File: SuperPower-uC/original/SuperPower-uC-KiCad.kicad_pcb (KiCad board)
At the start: 2 copper layers, 95 x 42 mm, 168 parts, among them J1 JST_PH_S2B_thru, J2 Barrel_Jack_Switch, J3 Conn_01x02_Male, J4 DNP/JST_ZH_S2B_thru, J5 JST_XH_S2B_thru, J6 Conn_01x02_Male, J7 mcu_pinout, J8 mcu_pinout, Q1 DMN2019UTS, Q10 2N7002A, Q11 2N7002A, Q12 DMP2035UVT, Q13 DMP2035UVT, Q14 DMP2035UVT, Q2 DMP3028LSD, Q3 DMN3018SSD, Q4 2N7002A, Q5 DMP2035UVT, Q6 BSS84-7-F, Q7 S8050, Q8 S8050, Q9 2N7002A, SW1 DNP/SKRKAEE020, U1 AP9101CK6-AYTRG1, U10 TPS63070RNMT, U2 USB-C, U3 IP4220CZ6, U4 LTC4162EUFD-LAD, U5 RV-3028-C7, U6 CP2102N-A01-GQFN28, U7 ESP32-WROOM32, U8 TPS70933DRVT, U9 TPS63070RNMT

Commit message: Update DMN3018SSD SO-8 3D Package
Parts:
- Q3: footprint Package_SO:SO-8_3.9x4.9mm_P1.27mm -> DMN3018SSD:SO-8_3.9x4.9mm_P1.27mm

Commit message: Update 18650 Battery Holder 3D Model
+ Board 3D Model + 3D box
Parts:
- BT1: footprint Battery:BatteryHolder_Keystone_1042_1x18650 -> BATTERY_CELL_HOLDER_18650_SMT_1042:BatteryHolder_Keystone_1042_1x18650

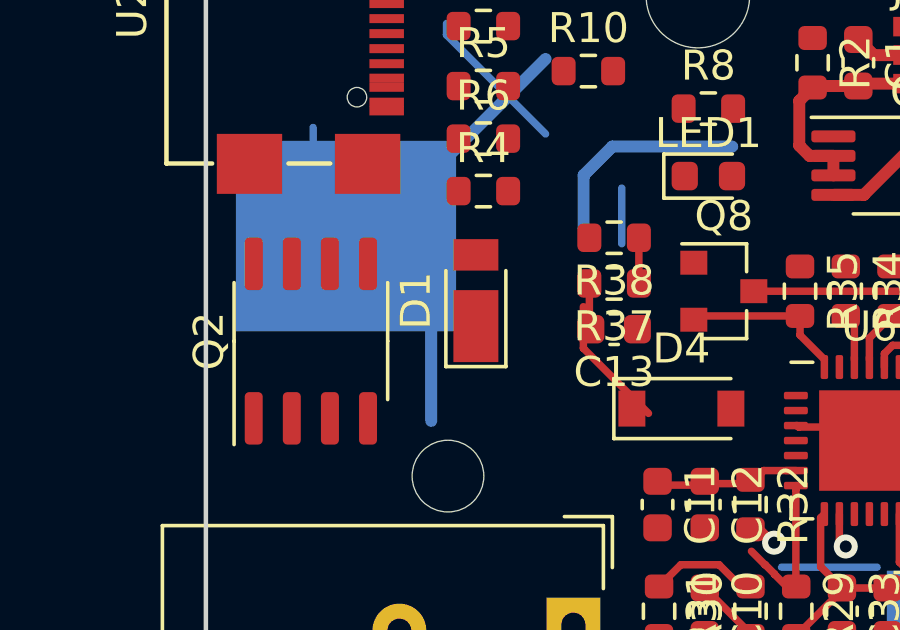
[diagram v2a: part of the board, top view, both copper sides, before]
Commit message: Add a second optional Schottky diode for High Current
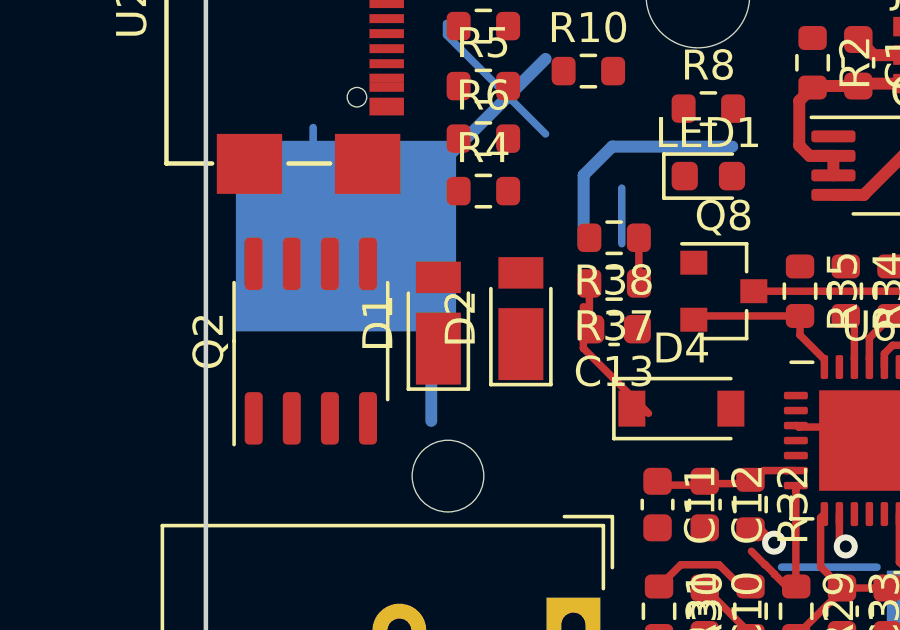
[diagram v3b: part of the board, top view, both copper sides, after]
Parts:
- added D2: DFLS230L, Diode_SMD:D_PowerDI-123, F.Cu at (120.5, 57.8)
- moved D1 1.46 mm to (117.8, 57.9)

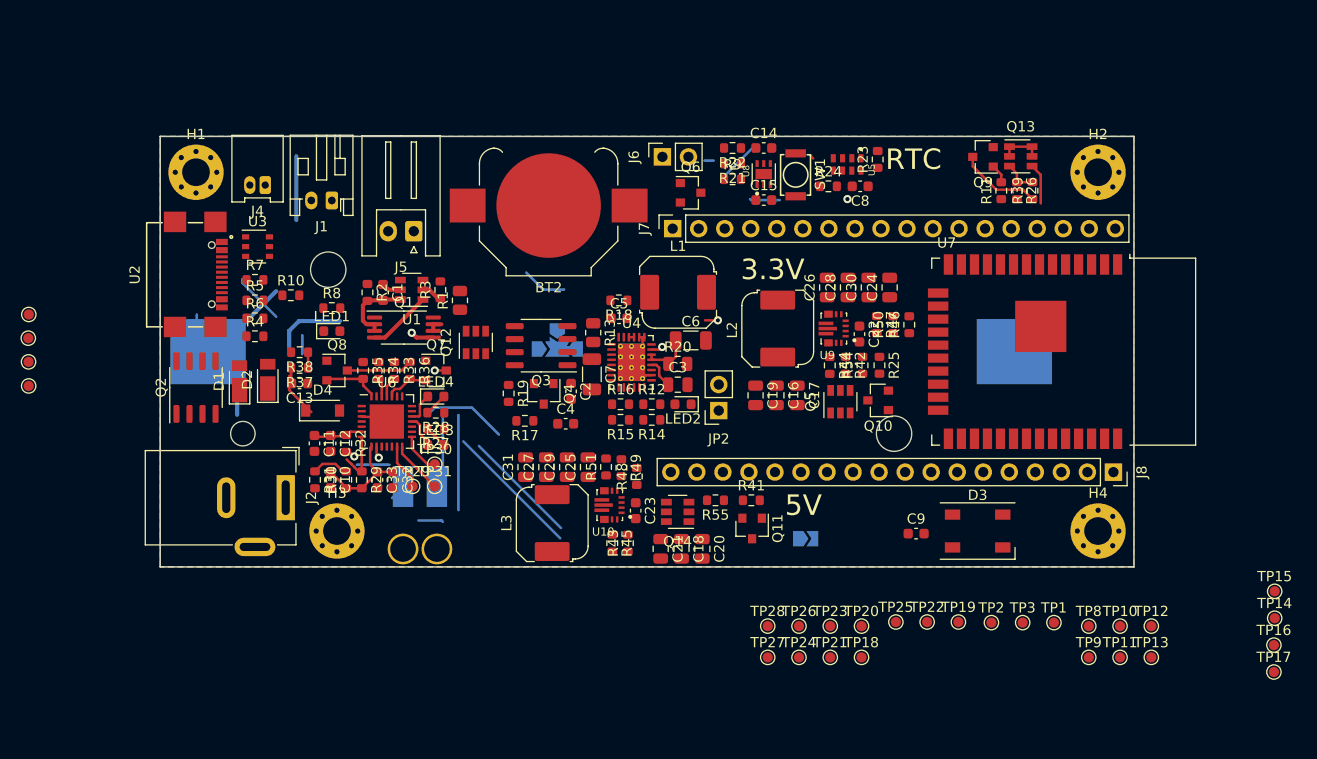
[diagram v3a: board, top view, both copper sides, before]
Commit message: Update components Placement
RTC + 3.3 LDO + single raw connectors (x2)
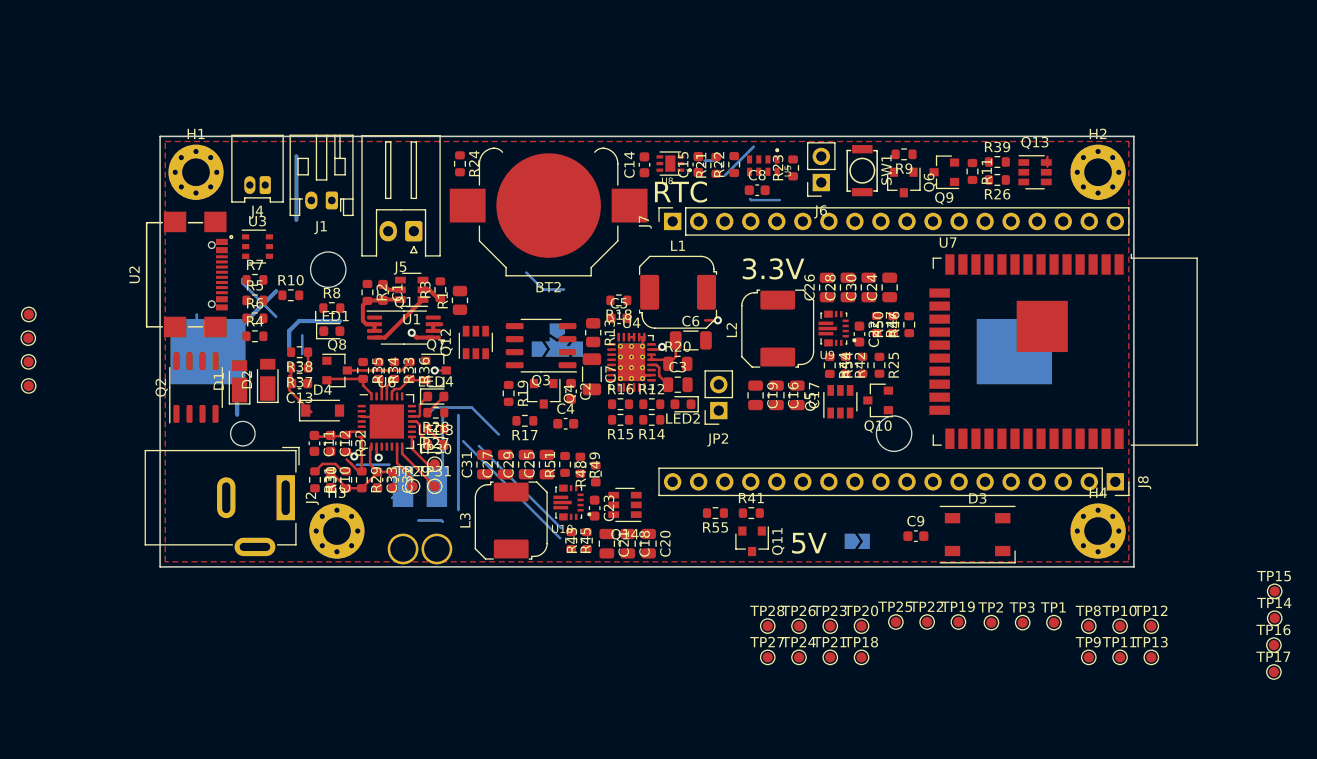
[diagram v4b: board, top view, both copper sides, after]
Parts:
- moved R24 36.0 mm to (139.2, 36.7), turned to 270 degrees
- moved Q6 20.8 mm to (182.6, 38.5), turned to 270 degrees
- moved R9 16.9 mm to (182.6, 35.8), turned to 180 degrees
- moved J6 15.7 mm to (174.5, 38.5), turned to 180 degrees
- moved C14 11.8 mm to (157.2, 36.8), turned to 90 degrees
- moved C8 10.1 mm to (168.2, 39.2), turned to 0 degrees
- moved U8 9.17 mm to (159.8, 36.6), turned to 180 degrees
- moved R23 8.29 mm to (171.8, 37.1)
- moved U5 8.17 mm to (168.8, 36.9)
- moved C15 7.27 mm to (162.5, 36.8), turned to 90 degrees
- moved SW1 6.51 mm to (178.5, 37.3)
- moved C18 5.27 mm to (155.6, 73.7)
- moved C20 5.27 mm to (157.6, 73.7)
- moved C21 5.27 mm to (153.6, 73.7)
- moved Q14 5.18 mm to (155.3, 70.0)
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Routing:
- net Net-(Q9-Pad3): track 8.07 -> 0.00 mm
- net /MCU Module/3v3_MCU: track 5.95 -> 1.52 mm
- net Net-(Q13-Pad3): track 3.40 -> 0.00 mm
- net /MCU Module/3v3: track 4.10 -> 0.95 mm
- net /MCU Module/EN_3V3: track 1.85 -> 0.00 mm
- net /Charging Module/3v3_I2C: vias 1 -> 0

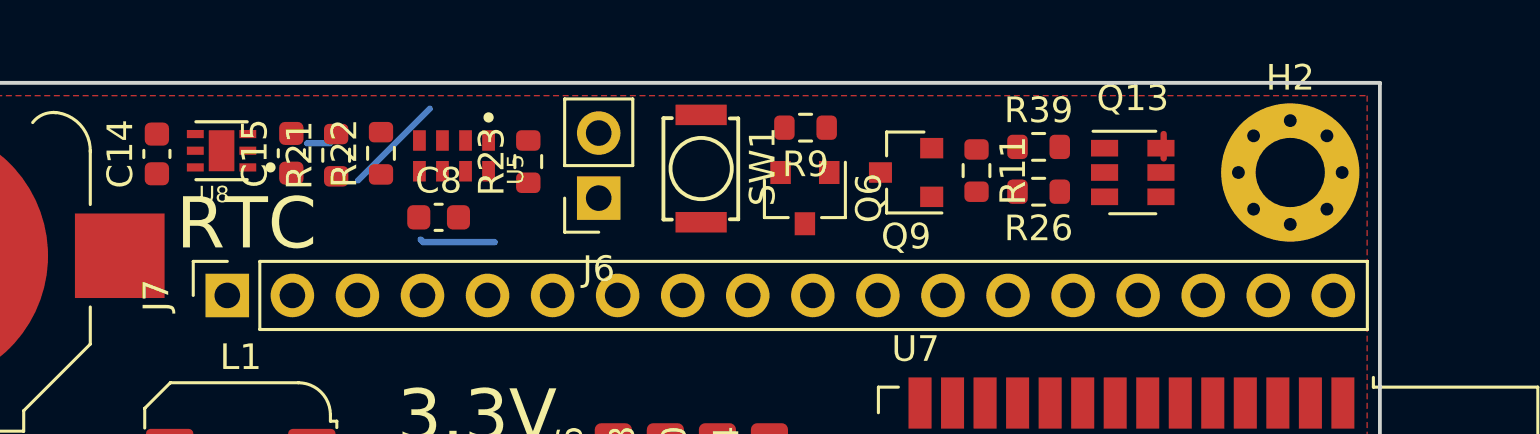
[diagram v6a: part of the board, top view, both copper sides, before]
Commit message: Update TPS709xx series 3D footprint
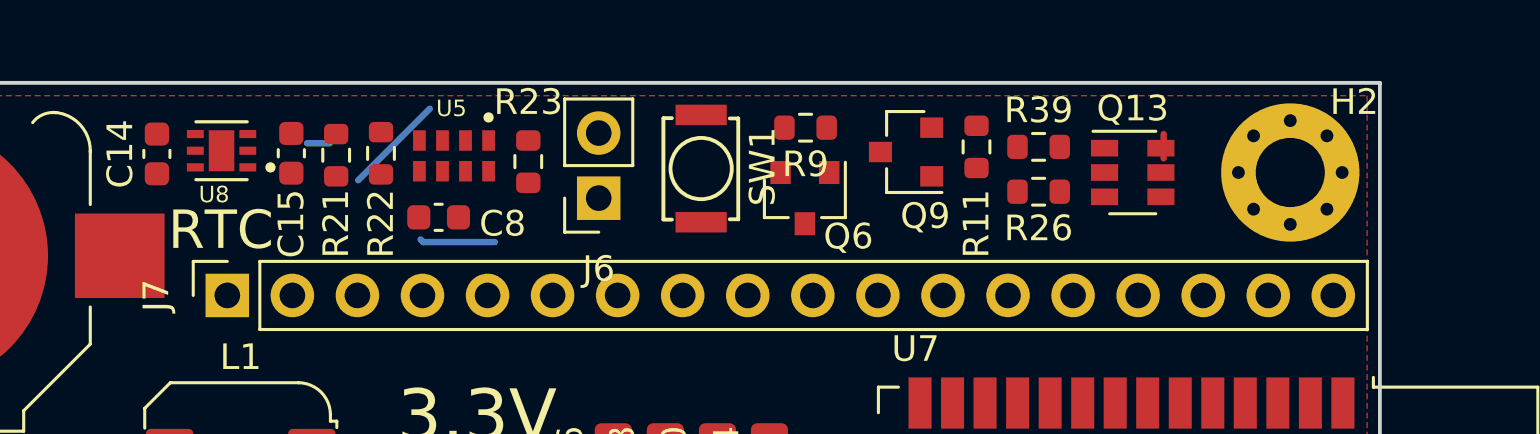
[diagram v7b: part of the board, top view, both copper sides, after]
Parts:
- moved R11 0.92 mm to (189.2, 36.5)
- moved Q9 0.80 mm to (186.5, 36.7)
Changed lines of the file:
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@@
     (uvia_drill 0.1)
   )
+  (module TPS70933DRV:SON65P200X200X80-7N (layer F.Cu)
+    (at 159.775 36.65 180)
+    (fp_text reference U8 (at 0.292 -1.7134) (layer F.SilkS)
+      (effects (font (size 0.64 0.64) (thickness 0.015)))
+    )
+    (fp_text value TPS70933DRVT (at 5.9816 1.7134) (layer F.Fab)
+      (effects (font (size 0.64 0.64) (thickness 0.015)))
+    )
+    (fp_poly (pts (xy -0.316 -0.506) (xy 0.316 -0.506) (xy 0.316 0.506) (xy -0.316 0.506)) (layer F.Paste) (width 0.01))
+    (fp_line (start 1.675 -1.25) (end 1.675 1.25) (layer F.CrtYd) (width 0.05))
+    (fp_line (start -1.675 -1.25) (end -1.675 1.25) (layer F.CrtYd) (width 0.05))
+    (fp_line (start -1.675 1.25) (end 1.675 1.25) (layer F.CrtYd) (width 0.05))
+    (fp_line (start -1.675 -1.25) (end 1.675 -1.25) (layer F.CrtYd) (width 0.05))
+    (fp_line (start 1 -1) (end 1 1) (layer F.Fab) (width 0.127))
+    (fp_line (start -1 -1) (end -1 1) (layer F.Fab) (width 0.127))
+    (fp_line (start -1 1.13) (end 1 1.13) (layer F.SilkS) (width 0.127))
+    (fp_line (start -1 -1.13) (end 1 -1.13) (layer F.SilkS) (width 0.127))
+    (fp_line (start -1 1) (end 1 1) (layer F.Fab) (width 0.127))
+    (fp_line (start -1 -1) (end 1 -1) (layer F.Fab) (width 0.127))
+    (fp_circle (center -1.91 -0.65) (end -1.81 -0.65) (layer F.Fab) (width 0.2))
+    (fp_circle (center -1.91 -0.65) (end -1.81 -0.65) (layer F.SilkS) (width 0.2))
+    (pad 7 smd rect (at 0 0 180) (size 1 1.6) (layers F.Cu F.Mask))
+    (pad 6 smd rect (at 1.025 -0.65 180) (size 0.66 0.32) (layers F.Cu F.Paste F.Mask)
+      (net 133 /RTC/VIN))
+    (pad 5 smd rect (at 1.025 0 180) (size 0.66 0.32) (layers F.Cu F.Paste F.Mask))
+    (pad 4 smd rect (at 1.025 0.65 180) (size 0.66 0.32) (layers F.Cu F.Paste F.Mask)
+      (net 127 "Net-(U8-Pad4)"))
+    (pad 3 smd rect (at -1.025 0.65 180) (size 0.66 0.32) (layers F.Cu F.Paste F.Mask)
+      (net 4 GND))
+    (pad 2 smd rect (at -1.025 0 180) (size 0.66 0.32) (layers F.Cu F.Paste F.Mask))
+    (pad 1 smd rect (at -1.025 -0.65 180) (size 0.66 0.32) (layers F.Cu F.Paste F.Mask)
+      (net 14 "/Charging Module/3v3_I2C"))
+    (model ${KISYS3DMOD}/Package_SON.3dshapes/WSON-6-1EP_2x2mm_P0.65mm_EP1x1.6mm.step
+      (at (xyz 0 0 0))
+      (scale (xyz 1 1 1))
+      (rotate (xyz 0 0 0))
+    )
+  )
   (module RV-3028-C7:IC_RV-3028-C7 (layer F.Cu)
     (at 168.85 36.85 270)
-    (fp_text reference U5 (at 0.532 -2.4064 90) (layer F.SilkS)
+    (fp_text reference U5 (at -1.85 0.1 180) (layer F.SilkS)
       (effects (font (size 0.64 0.64) (thickness 0.015)))
     )
@@
     (tags SOT-23-6)
     (attr smd)
-    (fp_text reference Q13 (at 0 -2.9) (layer F.SilkS)
+    (fp_text reference Q13 (at 0 -2.5) (layer F.SilkS)
       (effects (font (size 1 1) (thickness 0.15)))
     )
@@
     )
   )
-  (module TPS70933DRV:SON65P200X200X80-7N (layer F.Cu)
-    (at 159.775 36.65 180)
-    (fp_text reference U8 (at 0.292 -1.7134) (layer F.SilkS)
-      (effects (font (size 0.64 0.64) (thickness 0.015)))
-    )
-    (fp_text value TPS70933DRVT (at 5.9816 1.7134) (layer F.Fab)
-      (effects (font (size 0.64 0.64) (thickness 0.015)))
-    )
-    (fp_poly (pts (xy -0.316 -0.506) (xy 0.316 -0.506) (xy 0.316 0.506) (xy -0.316 0.506)) (layer F.Paste) (width 0.01))
-    (fp_line (start 1.675 -1.25) (end 1.675 1.25) (layer F.CrtYd) (width 0.05))
-    (fp_line (start -1.675 -1.25) (end -1.675 1.25) (layer F.CrtYd) (width 0.05))
-    (fp_line (start -1.675 1.25) (end 1.675 1.25) (layer F.CrtYd) (width 0.05))
-    (fp_line (start -1.675 -1.25) (end 1.675 -1.25) (layer F.CrtYd) (width 0.05))
-    (fp_line (start 1 -1) (end 1 1) (layer F.Fab) (width 0.127))
-    (fp_line (start -1 -1) (end -1 1) (layer F.Fab) (width 0.127))
-    (fp_line (start -1 1.13) (end 1 1.13) (layer F.SilkS) (width 0.127))
-    (fp_line (start -1 -1.13) (end 1 -1.13) (layer F.SilkS) (width 0.127))
-    (fp_line (start -1 1) (end 1 1) (layer F.Fab) (width 0.127))
-    (fp_line (start -1 -1) (end 1 -1) (layer F.Fab) (width 0.127))
-    (fp_circle (center -1.91 -0.65) (end -1.81 -0.65) (layer F.Fab) (width 0.2))
-    (fp_circle (center -1.91 -0.65) (end -1.81 -0.65) (layer F.SilkS) (width 0.2))
-    (pad 7 smd rect (at 0 0 180) (size 1 1.6) (layers F.Cu F.Mask))
-    (pad 6 smd rect (at 1.025 -0.65 180) (size 0.66 0.32) (layers F.Cu F.Paste F.Mask)
-      (net 133 /RTC/VIN))
-    (pad 5 smd rect (at 1.025 0 180) (size 0.66 0.32) (layers F.Cu F.Paste F.Mask))
-    (pad 4 smd rect (at 1.025 0.65 180) (size 0.66 0.32) (layers F.Cu F.Paste F.Mask)
-      (net 127 "Net-(U8-Pad4)"))
-    (pad 3 smd rect (at -1.025 0.65 180) (size 0.66 0.32) (layers F.Cu F.Paste F.Mask)
-      (net 4 GND))
-    (pad 2 smd rect (at -1.025 0 180) (size 0.66 0.32) (layers F.Cu F.Paste F.Mask))
-    (pad 1 smd rect (at -1.025 -0.65 180) (size 0.66 0.32) (layers F.Cu F.Paste F.Mask)
-      (net 14 "/Charging Module/3v3_I2C"))
-  )
   (module Resistor_SMD:R_0603_1608Metric (layer F.Cu)
     (at 191.675 36.5)
@@
   )
   (module Resistor_SMD:R_0603_1608Metric (layer F.Cu)
-    (at 189.25 37.425 270)
+    (at 189.25 36.5 270)
     (descr "Resistor SMD 0603 (1608 Metric), square (rectangular) end terminal, IPC_7351 nominal, (Body size source: IPC-SM-782 page 72, https://www.pcb-3d.com/wordpress/wp-content/uploads/ipc-sm-782a_amendment_1_and_2.pdf), generated with kicad-footprint-generator")
     (tags resistor)
     (attr smd)
-    (fp_text reference R11 (at 0 -1.43 90) (layer F.SilkS)
+    (fp_text reference R11 (at 3 0 90) (layer F.SilkS)
       (effects (font (size 1 1) (thickness 0.15)))
     )
@@
   )
   (module Package_TO_SOT_SMD:SOT-23 (layer F.Cu)
-    (at 186.5 37.5 180)
+    (at 186.5 36.7 180)
     (descr "SOT-23, Standard")
     (tags SOT-23)
     (attr smd)
-    (fp_text reference Q9 (at 0 -2.5) (layer F.SilkS)
+    (fp_text reference Q9 (at -0.75 -2.5) (layer F.SilkS)
       (effects (font (size 1 1) (thickness 0.15)))
     )
@@
     (tags SOT-23)
     (attr smd)
-    (fp_text reference Q6 (at 0 -2.5 90) (layer F.SilkS)
+    (fp_text reference Q6 (at 1.5 -1.7 180) (layer F.SilkS)
       (effects (font (size 1 1) (thickness 0.15)))
     )
@@
     (tags capacitor)
     (attr smd)
-    (fp_text reference C15 (at 0 -1.43 90) (layer F.SilkS)
+    (fp_text reference C15 (at -2.75 0 90) (layer F.SilkS)
       (effects (font (size 1 1) (thickness 0.15)))
     )
@@
     (tags resistor)
     (attr smd)
-    (fp_text reference R23 (at 0 -1.43 90) (layer F.SilkS)
+    (fp_text reference R23 (at 2.325 0 180) (layer F.SilkS)
       (effects (font (size 1 1) (thickness 0.15)))
     )
@@
     (tags resistor)
     (attr smd)
-    (fp_text reference R22 (at 0 -1.43 90) (layer F.SilkS)
+    (fp_text reference R22 (at -2.75 0 90) (layer F.SilkS)
       (effects (font (size 1 1) (thickness 0.15)))
     )
@@
     (tags resistor)
     (attr smd)
-    (fp_text reference R21 (at 0 -1.43 90) (layer F.SilkS)
+    (fp_text reference R21 (at -2.675 0 90) (layer F.SilkS)
       (effects (font (size 1 1) (thickness 0.15)))
     )
@@
     (tags capacitor)
     (attr smd)
-    (fp_text reference C8 (at 0 -1.43) (layer F.SilkS)
+    (fp_text reference C8 (at 2.5 0.25) (layer F.SilkS)
       (effects (font (size 1 1) (thickness 0.15)))
     )
@@
     (tags "mounting hole 2.7mm")
     (attr virtual)
-    (fp_text reference H2 (at 0 -3.7) (layer F.SilkS)
+    (fp_text reference H2 (at 2.5 -2.75) (layer F.SilkS)
       (effects (font (size 1 1) (thickness 0.15)))
     )
@@
   (gr_line (start 205 34) (end 205 76) (layer Edge.Cuts) (width 0.15))
   (gr_line (start 110 34) (end 205 34) (layer Edge.Cuts) (width 0.15))
-  (gr_text RTC (at 160.75 39.5) (layer F.SilkS)
-    (effects (font (size 2 2) (thickness 0.15)))
+  (gr_text RTC (at 159.75 39.75) (layer F.SilkS)
+    (effects (font (size 1.5 1.5) (thickness 0.15)))
   )
   (gr_text 3.3V (at 169.75 47) (layer F.SilkS)
